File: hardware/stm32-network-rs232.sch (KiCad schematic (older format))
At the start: 24 parts, among them J101 USB, M101 Mount Hole, M102 Mount Hole, M103 Mount Hole, M104 Mount Hole, P101 DEBUG, U101 MOSFET-P, U102 STM32-48PIN, X101 8MHz

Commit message: max3221
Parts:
- added C? (x4): 0.1uF, symbol C
- added U?: MAX3221, symbol MAX3221
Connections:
- net +3.3V: now also U?.12 (FORCEON), U?.15 (VCC), U?.16 (~FORCEOFF)
- net GNDPWR: now also C?.2, C?.2, U?.1 (~EN), U?.14 (GND)
- net USART1RX: now also U?.9 (ROUT)
- net USART1TX: now also U?.11 (DIN)
- new net: C?.1, U?.2 (C1+)
- new net: C?.2, U?.4 (C1-)
- new net: C?.1, U?.3 (V+)
- new net: C?.1, U?.5 (C2+)
- new net: C?.2, U?.6 (C2-)
- new net: C?.1, U?.7 (V-)
- no-connect marks 9 -> 10

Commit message: fix pins
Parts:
- added C?: 0.1uF, symbol C
- added P104: RS-232-DB-9-DTE, symbol RS-232-DB-9-DTE
- gave numbers to parts that had none: 7
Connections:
- net +3.3V: now also C?.1
- net GNDPWR: now also C?.2, P104.10 (CASE), P104.5 (GND)
- net at U103.13 (DOUT): now also P104.2 (RXD)
- net at U103.8 (RIN): now also P104.3 (TXD)
- no-connect marks 10 -> 16
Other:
- moved on the sheet: C103, C104, C110, C111, C112, C113, J101, P101, P102, P103, R101, R102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

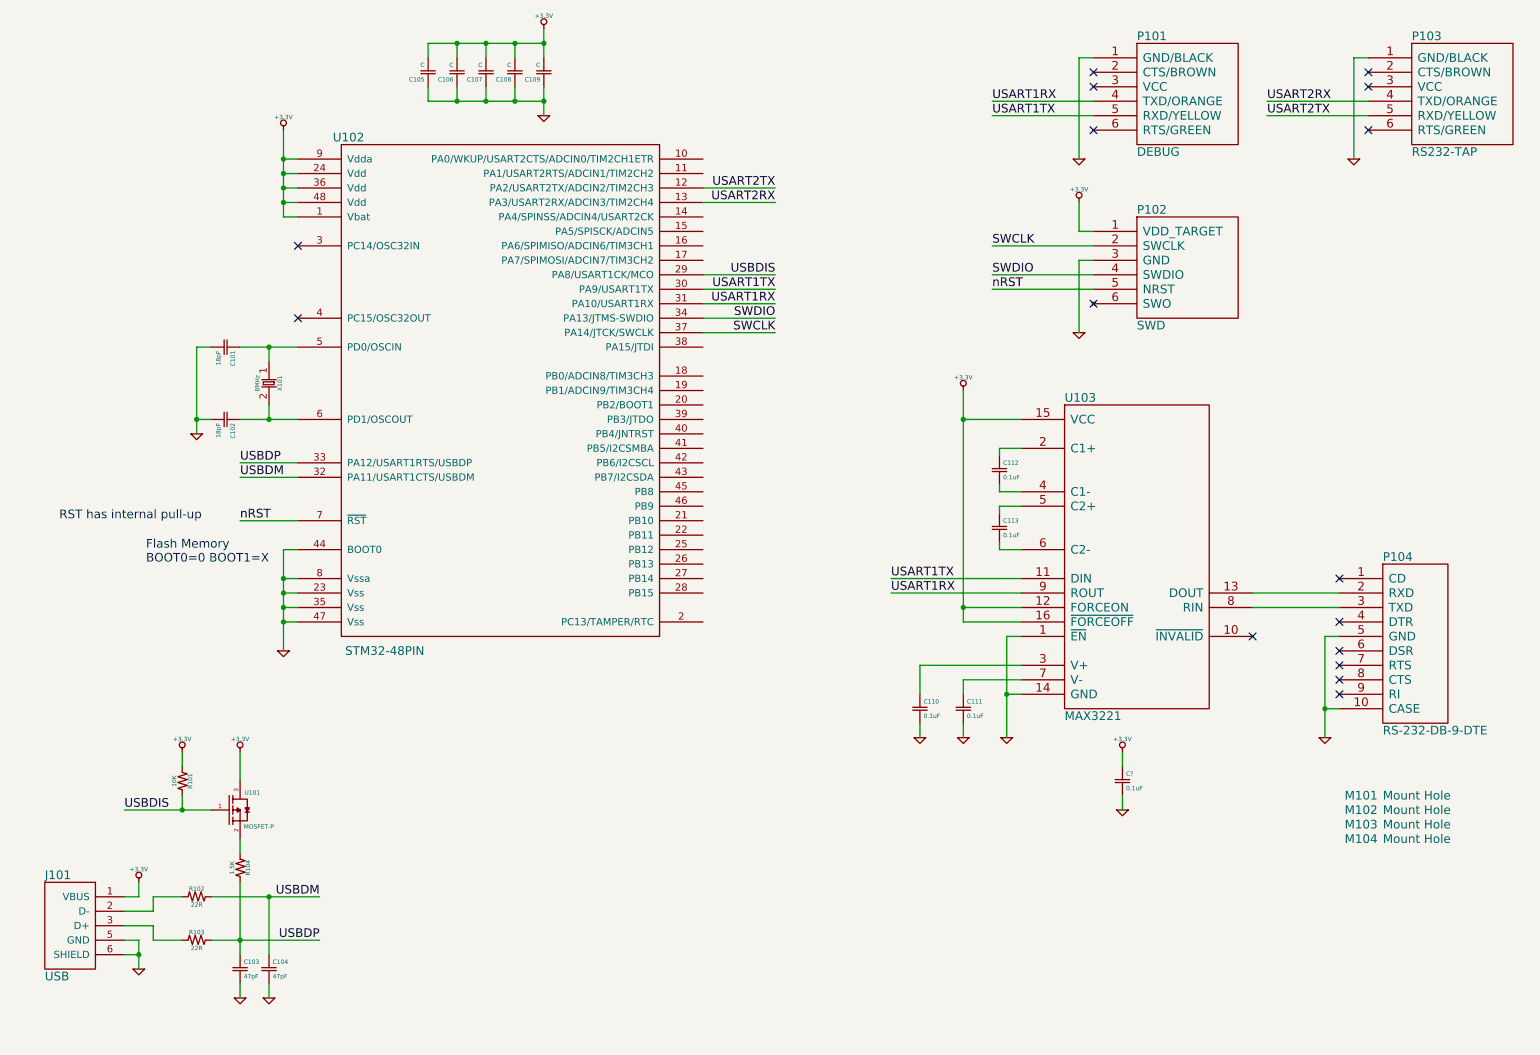
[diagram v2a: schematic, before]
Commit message: BELFUSE-08B0-1X1T-06-F
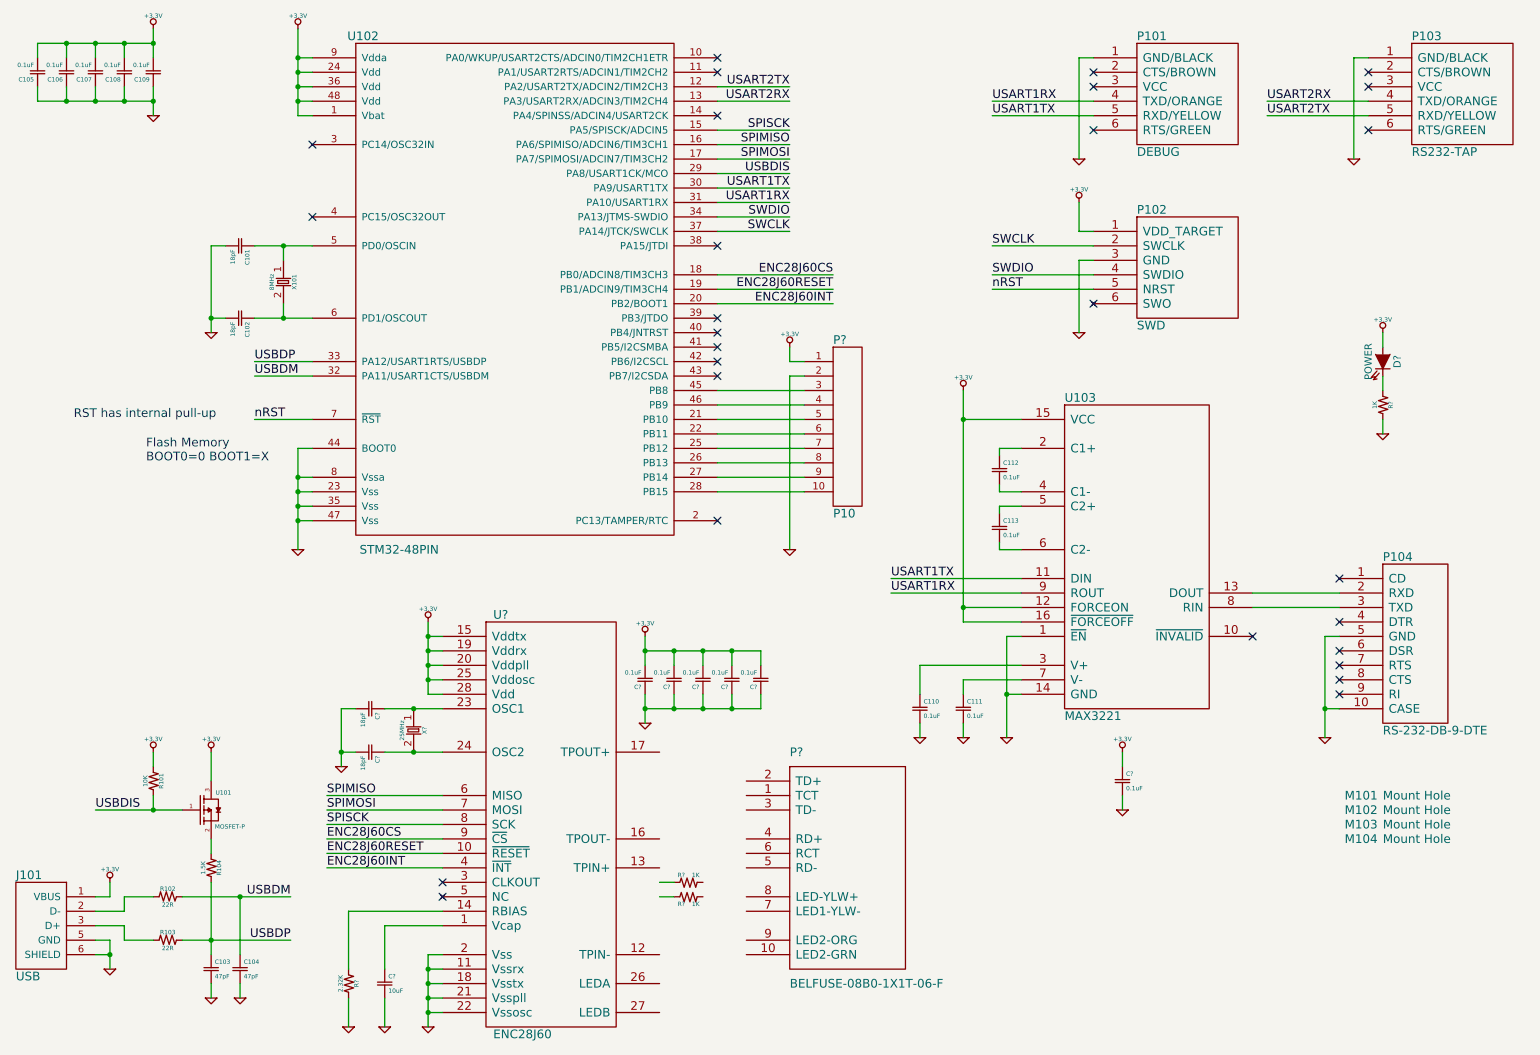
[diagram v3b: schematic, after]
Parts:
- added C? (x2): 18pF, symbol C
- added C?: 10uF, symbol C
- added C? (x5): 0.1uF, symbol C
- added D?: POWER, symbol LED
- added P?: P10, symbol P10
- added P?: BELFUSE-08B0-1X1T-06-F, symbol BELFUSE-08B0-1X1T-06-F
- added R? (x3): 1K, symbol R
- added R?: 2.32K, symbol R
- added U?: ENC28J60, symbol ENC28J60
- added X?: 25MHz, symbol CRYSTAL
- C105, C106, C107, C108, C109: value C -> 0.1uF
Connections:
- net +3.3V: now also C?.2, C?.2, C?.2, C?.2, C?.2, D?.1 (A), P?.1, U?.15 (Vddtx), U?.19 (Vddrx), U?.20 (Vddpll), U?.25 (Vddosc), U?.28 (Vdd)
- net GNDPWR: now also C?.1, C?.1, C?.1, C?.1, C?.1, C?.2, C?.2, C?.2, P?.2, R?.1, R?.1, U?.11 (Vssrx), U?.18 (Vsstx), U?.2 (Vss), U?.21 (Vsspll), U?.22 (Vssosc)
- net SPISCK: now reaches U102.15 (PA5/SPISCK/ADCIN5)
- net SPISCK: now also U?.8 (SCK)
- net SPIMISO: now reaches U102.16 (PA6/SPIMISO/ADCIN6/TIM3CH1)
- net SPIMISO: now also U?.6 (MISO)
- net SPIMOSI: now reaches U102.17 (PA7/SPIMOSI/ADCIN7/TIM3CH2)
- net SPIMOSI: now also U?.7 (MOSI)
- net ENC28J60CS: now reaches U102.18 (PB0/ADCIN8/TIM3CH3)
- net ENC28J60CS: now also U?.9 (~CS)
- net ENC28J60RESET: now reaches U102.19 (PB1/ADCIN9/TIM3CH4)
- net ENC28J60RESET: now also U?.10 (~RESET)
- net ENC28J60INT: now reaches U102.20 (PB2/BOOT1)
- net ENC28J60INT: now also U?.4 (~INT)
- net at U102.21 (PB10): now also P?.5
- net at U102.22 (PB11): now also P?.6
- net at U102.25 (PB12): now also P?.7
- net at U102.26 (PB13): now also P?.8
- net at U102.27 (PB14): now also P?.9
- net at U102.28 (PB15): now also P?.10
- net at U102.45 (PB8): now also P?.3
- net at U102.46 (PB9): now also P?.4
- new net: D?.2 (K), R?.2
- new net: C?.1, U?.23 (OSC1), X?.1
- new net: C?.1, U?.24 (OSC2), X?.2
- new net: C?.1, U?.1 (Vcap)
- new net: R?.2, U?.14 (RBIAS)
- no-connect marks 16 -> 28
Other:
- moved on the sheet: C101, C102, C103, C104, C105, C106, C107, C108, C109, J101, R101, R102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

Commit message: schematic complete
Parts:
- removed R? (x2): 1K, symbol R
- added C? (x2): 0.1uF, symbol C
- added L?: 10uH, symbol INDUCTOR
- added R? (x4): 50R, symbol R
- added R? (x2): 1K, symbol R
- R?: value 2.32K -> 2.32K 1%
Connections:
- net +3.3V: now also L?.1
- net GNDPWR: now also P?.7 (LED1-YLW-), P?.9 (LED2-ORG), C?.1, C?.1
- net at P?.1 (TCT): now also C?.2, L?.2, R?.1, R?.2
- net at P?.10 (LED2-GRN): now also R?.2
- net at P?.2 (TD+): now also U?.17 (TPOUT+), R?.2
- net at P?.3 (TD-): now also U?.16 (TPOUT-), R?.1
- net at P?.4 (RD+): now also U?.13 (TPIN+), R?.2
- net at P?.5 (RD-): now also U?.12 (TPIN-), R?.1
- net at P?.6 (RCT): now also C?.2, R?.1, R?.2
- net at P?.8 (LED-YLW+): now also R?.2
- net at U?.26 (LEDA): now also R?.1
- net at U?.27 (LEDB): now also R?.1
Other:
- moved on the sheet: C103, C104, C?, D?, J101, P?, R101, R102, R103, R104, R?, U101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

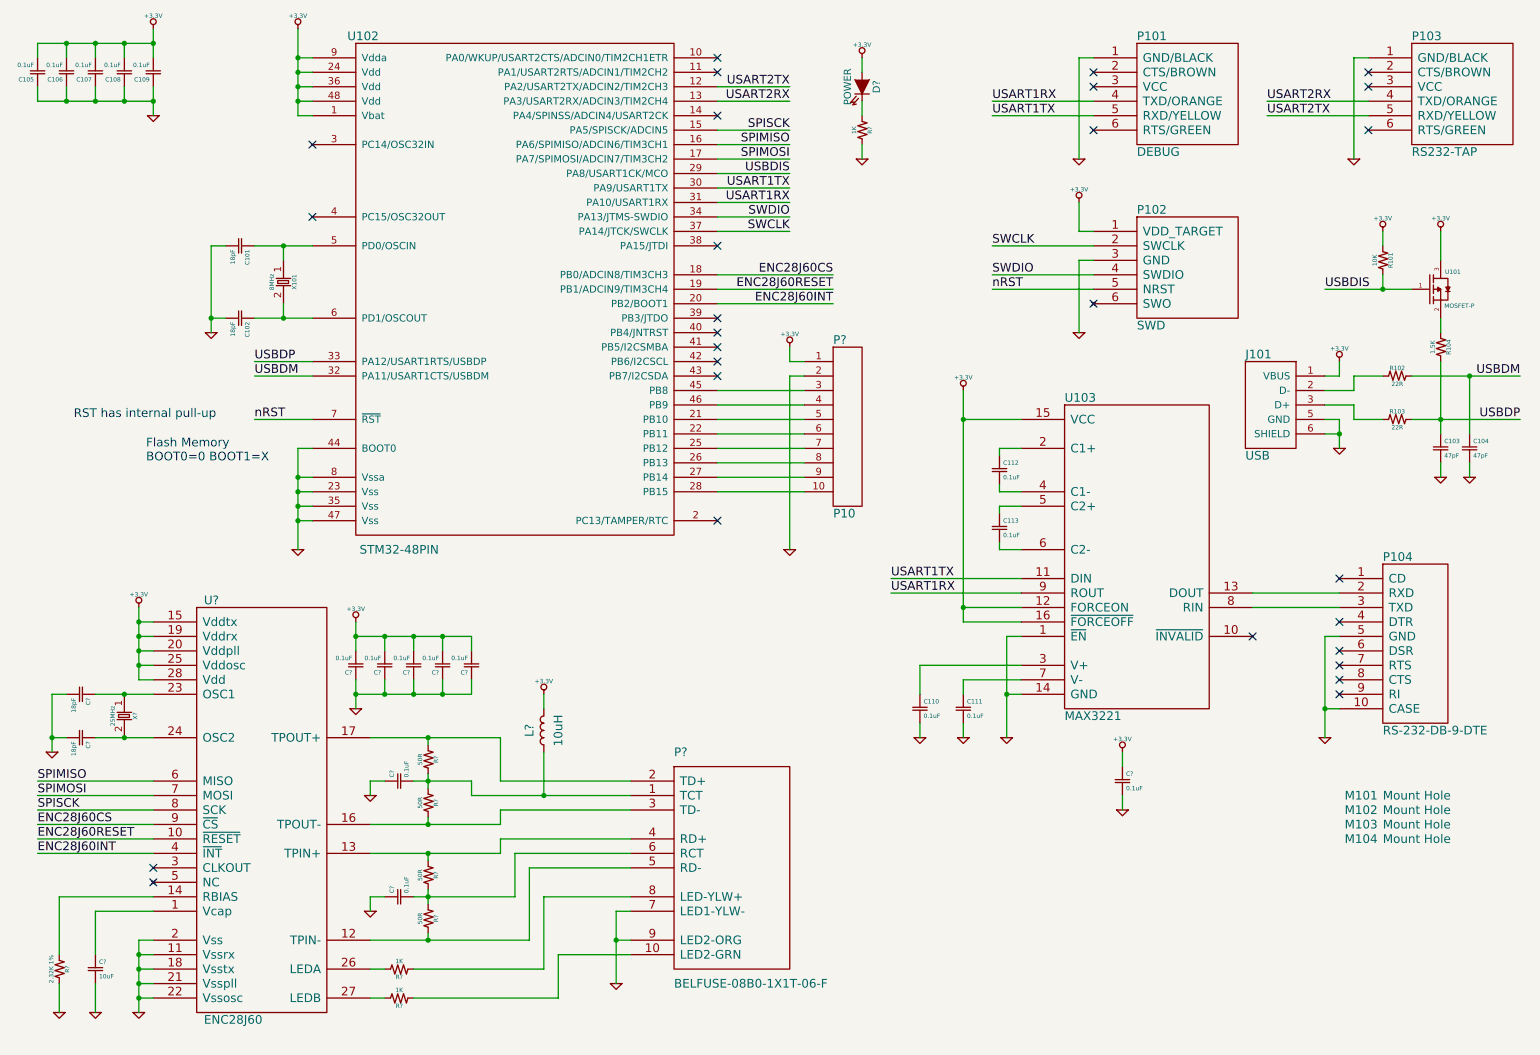
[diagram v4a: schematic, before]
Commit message: add 3.3V reg
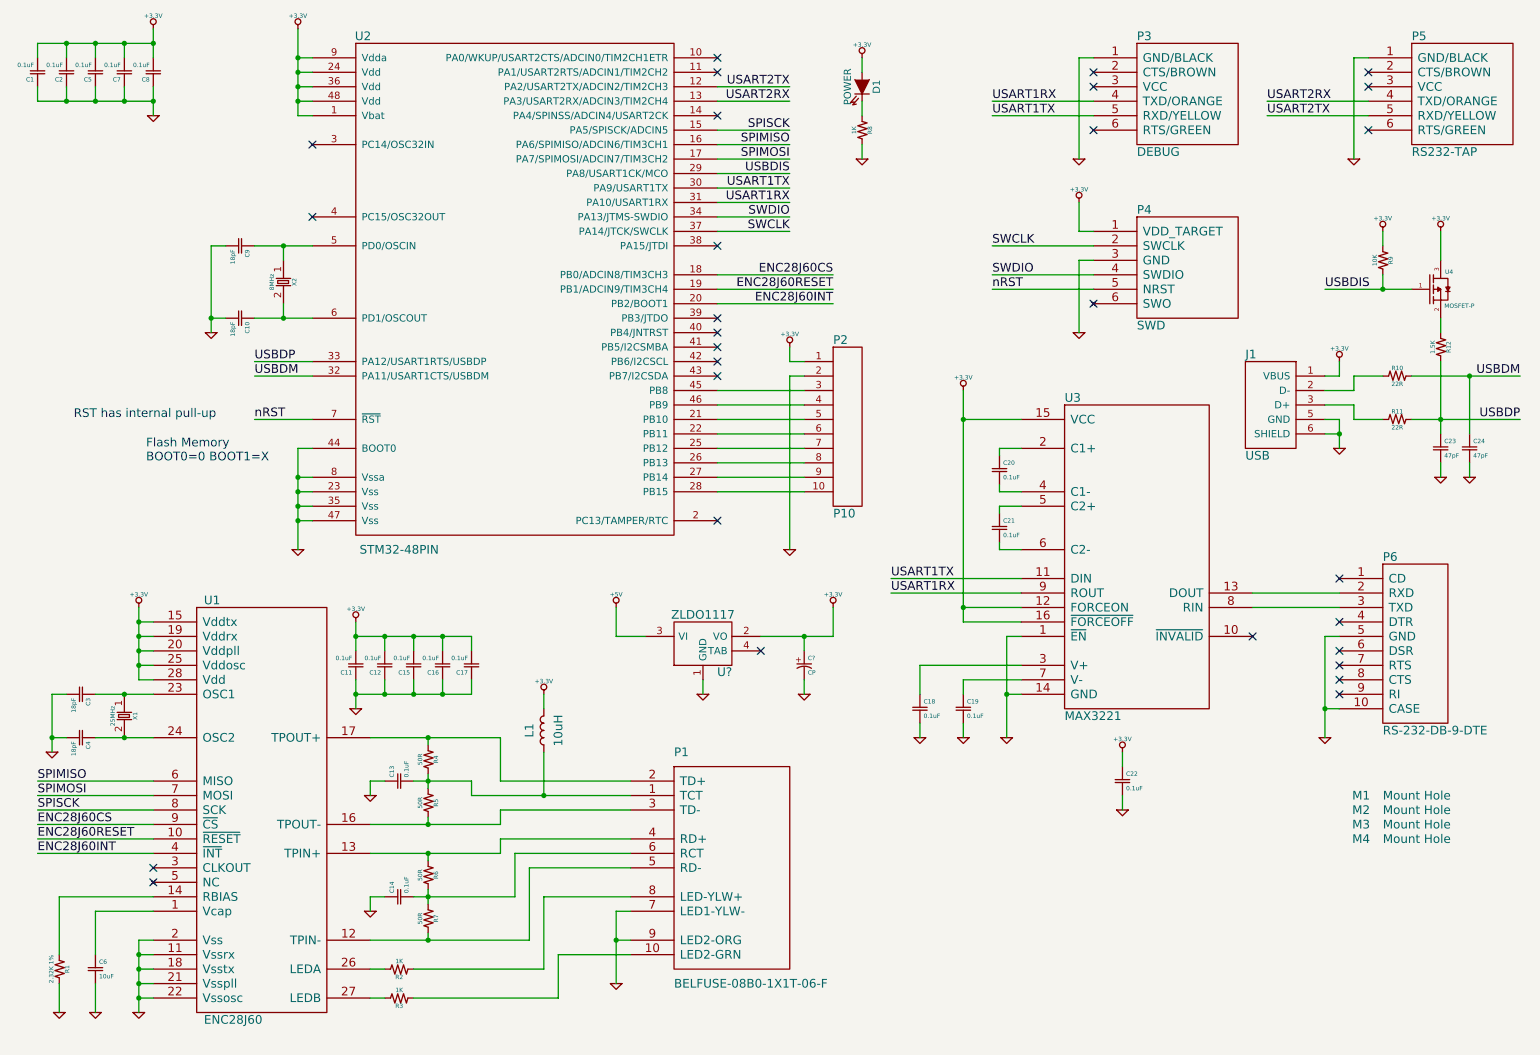
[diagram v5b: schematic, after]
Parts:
- added C?: CP, symbol CP
- added U?: ZLDO1117, symbol VREG_VOUTCENTER
- gave numbers to parts that had none: 25
- renumbered C105 to C1, C102 to C10, C110 to C18, C111 to C19, C106 to C2, C112 to C20, C113 to C21, C103 to C23, C104 to C24, C107 to C5, C108 to C7, C109 to C8, C101 to C9, J101 to J1, M101 to M1, M102 to M2, M103 to M3, M104 to M4, P101 to P3, P102 to P4, P103 to P5, P104 to P6, R102 to R10, R103 to R11, R104 to R12, R101 to R9, U102 to U2, U103 to U3, U101 to U4, X101 to X2
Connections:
- net +3.3V: now also C?.1, U?.2 (VO)
- net GNDPWR: now also C?.2, U?.1 (GND)
- new net +5V: U?.3 (VI)
- no-connect marks 28 -> 29
